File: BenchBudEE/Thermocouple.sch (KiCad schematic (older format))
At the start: 12 parts, among them U4 LM324, U5 MCP3550-50-E/MS, U6 MCP3550-50-E/MS, U7 LM324

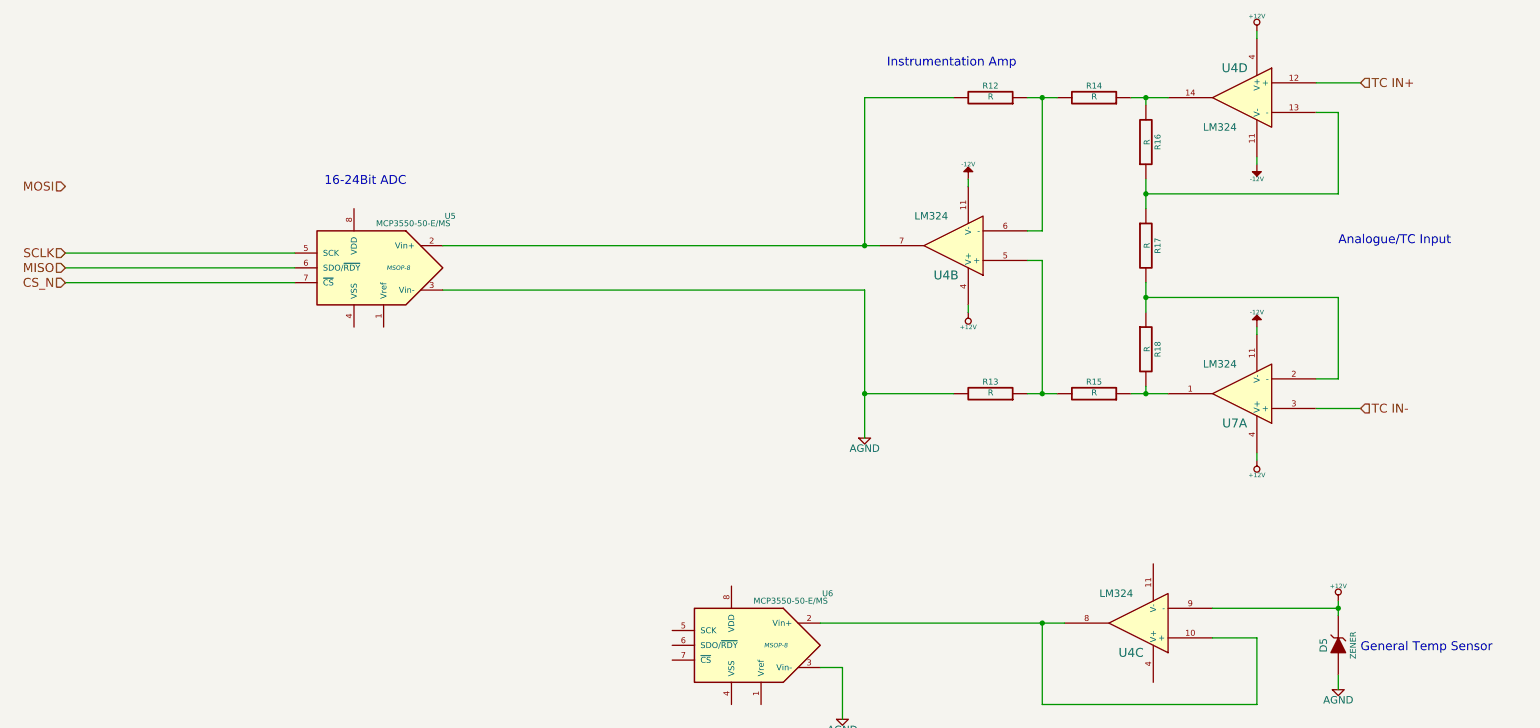
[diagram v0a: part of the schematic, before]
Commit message: Parts added to thermocouple module. Relay & thermocouple rough placement.
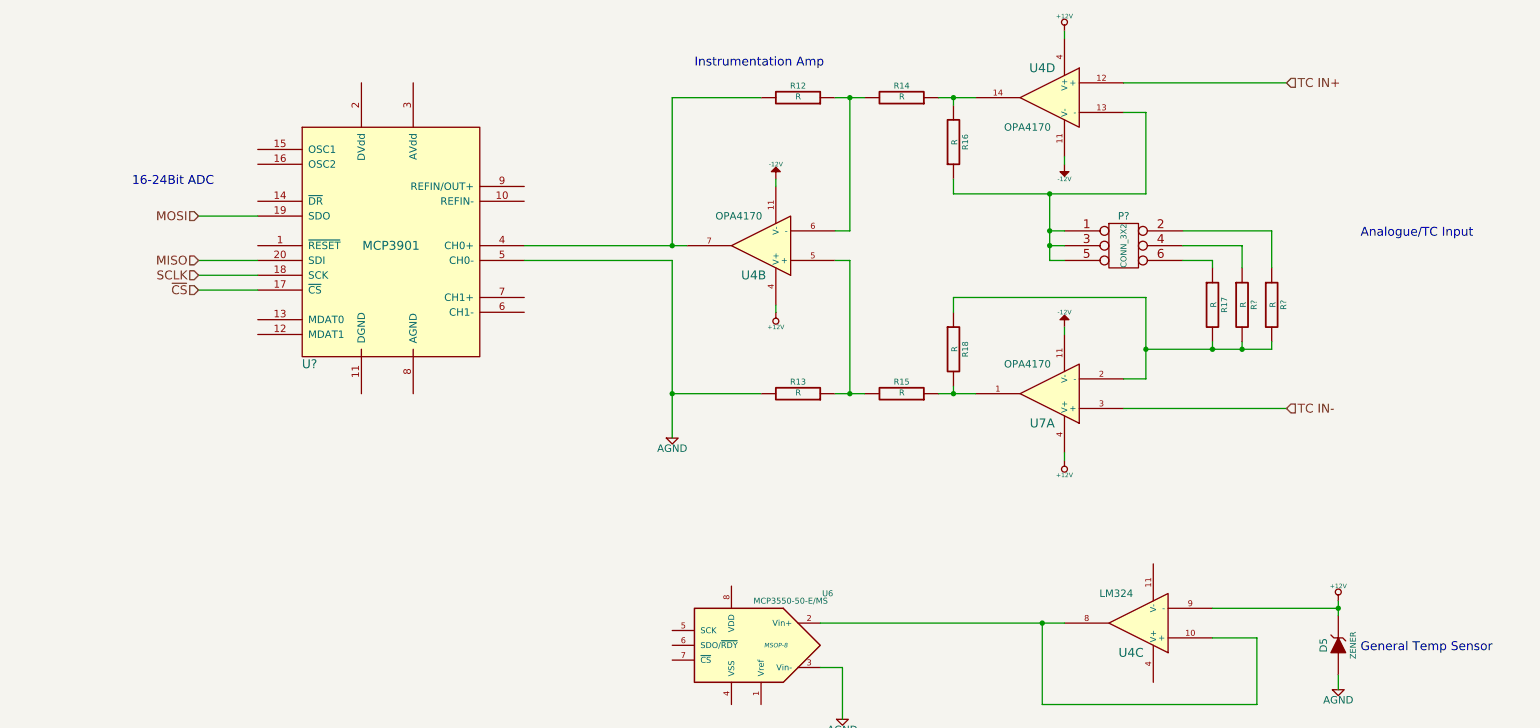
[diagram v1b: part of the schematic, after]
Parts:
- removed U5: MCP3550-50-E/MS, MSOP-8, symbol MCP3550-50-E/MS
- added P?: CONN_3X2, symbol CONN_3X2
- added R? (x2): R, ~, symbol R
- added U?: MCP3901, symbol MCP3901
- U4, U7: value LM324 -> OPA4170
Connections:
- net AGND: now also U?.5 (CH0-)
- net MISO: now also U?.20 (SDI)
- net MOSI: now also U?.19 (SDO)
- net SCLK: now also U?.18 (SCK)
- net at R17.2, R18.1, U7.2 (-): now also R?.2, R?.2
- net at R16.1, U4.13 (-): now also P?.1, P?.3, P?.5; no longer R17.1
- net at R12.2, U4.7: now also U?.4 (CH0+)
- new net: P?.6, R17.1
- new net: P?.4, R?.1
- new net: P?.2, R?.1
- new net ~CS: U?.17 (~CS)
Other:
- moved on the sheet: R12, R13, R14, R15, R16, R17, R18, U4B, U4D, U7A

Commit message: Arduino module associated + roughly placed.
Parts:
- removed unit 3 of U4
- removed U6: MCP3550-50-E/MS, MSOP-8, symbol MCP3550-50-E/MS
- added C10, C5, C6, C7, C8, C9: C, ~, symbol C
- added P3: CONN_2, symbol CONN_2
- added R47, R48: 0R, ~, symbol R
- added U6: LMT84, symbol LMT84
- D5: value ZENER -> LMT84; Distributor (none) -> DigiKey; Distributor Part Link (none) -> http://www.digikey.com/product-detail/en/LMT84DCKT/296-3572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; Distributor Part Number (none) -> 296-35727-2-ND; MFG Name (none) -> Texas Instruments; MFG Part Number (none) -> LMT84DCKT
- U4: Distributor (none) -> DigiKey; Distributor Part Link (none) -> www.digikey.com/product-detail/en/OPA4170AIDR/296-29664-1-N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; Distributor Part Number (none) -> 296-29664-1-ND; MFG Name (none) -> Texas Instruments; MFG Part Number (none) -> OPA4170AIDR
- U4: renamed from U7; Distributor (none) -> DigiKey; Distributor Part Link (none) -> www.digikey.com/product-detail/en/OPA4170AIDR/296-29664-1-N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; Distributor Part Number (none) -> 296-29664-1-ND; MFG Name (none) -> Texas Instruments; MFG Part Number (none) -> OPA4170AIDR
- gave numbers to parts that had none: 4
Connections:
- net +12V: now also C9.2
- net -12V: now also C8.2
- net AGND: now also U5.11 (DGND), U5.8 (AGND), C10.2, C6.1, C7.2, C8.1, C9.1, R47.1, R48.2, U6.1 (GND), U6.2 (GND), U6.5 (GND); no longer D5.1 (A), R13.2, U5.5 (CH0-)
- net MISO: now also U5.19 (SDO); no longer U5.20 (SDI)
- net MOSI: now also U5.20 (SDI); no longer U5.19 (SDO)
- net CH0+: now reaches R12.2, U4.7, U5.4 (CH0+)
- net CH0+: now also C5.1
- net ~RESET: now reaches U5.1 (~RESET)
- net REF-: now reaches U5.10 (REFIN-)
- net at U5.12 (MDAT1): now also P3.1 (P1)
- net at U5.13 (MDAT0): now also P3.2 (PM)
- net ~DR: now reaches U5.14 (~DR)
- net at U5.2 (DVdd): now also C6.2
- net +5V: now reaches U5.3 (AVdd)
- net +5V: now also C10.1, C7.1, U6.4 (Vdd)
- net CH1-: now reaches U5.6 (CH1-)
- net CH1-: now also R47.2
- net Ch1+: now reaches U5.7 (CH1+)
- net Ch1+: now also U6.3 (OUT)
- net REF+: now reaches U5.9 (REFIN/OUT+)
- new net CH0-: C5.2, R13.2, R48.1, U5.5 (CH0-)
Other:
- moved on the sheet: D5
